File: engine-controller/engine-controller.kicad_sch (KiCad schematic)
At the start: 0 parts

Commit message: inital TCs
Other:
- added sheet TC0 (thermocouple.kicad_sch)
- added sheet TC1 (thermocouple.kicad_sch)
- added sheet TC2 (thermocouple.kicad_sch)
- added sheet TC3 (thermocouple.kicad_sch)
- sheet STM32 ports: added PA10, PA11, PA12, PA8, PA9, PB12, PB13, PB14, PB15, PB5, PB6, PB7, PB8, PB9, PC0, PC1, PC2, PC3, PC6, PC7, PC8, PC9, SPI1_MISO, SPI1_MOSI, SPI1_NSS, SPI1_SCK; removed none

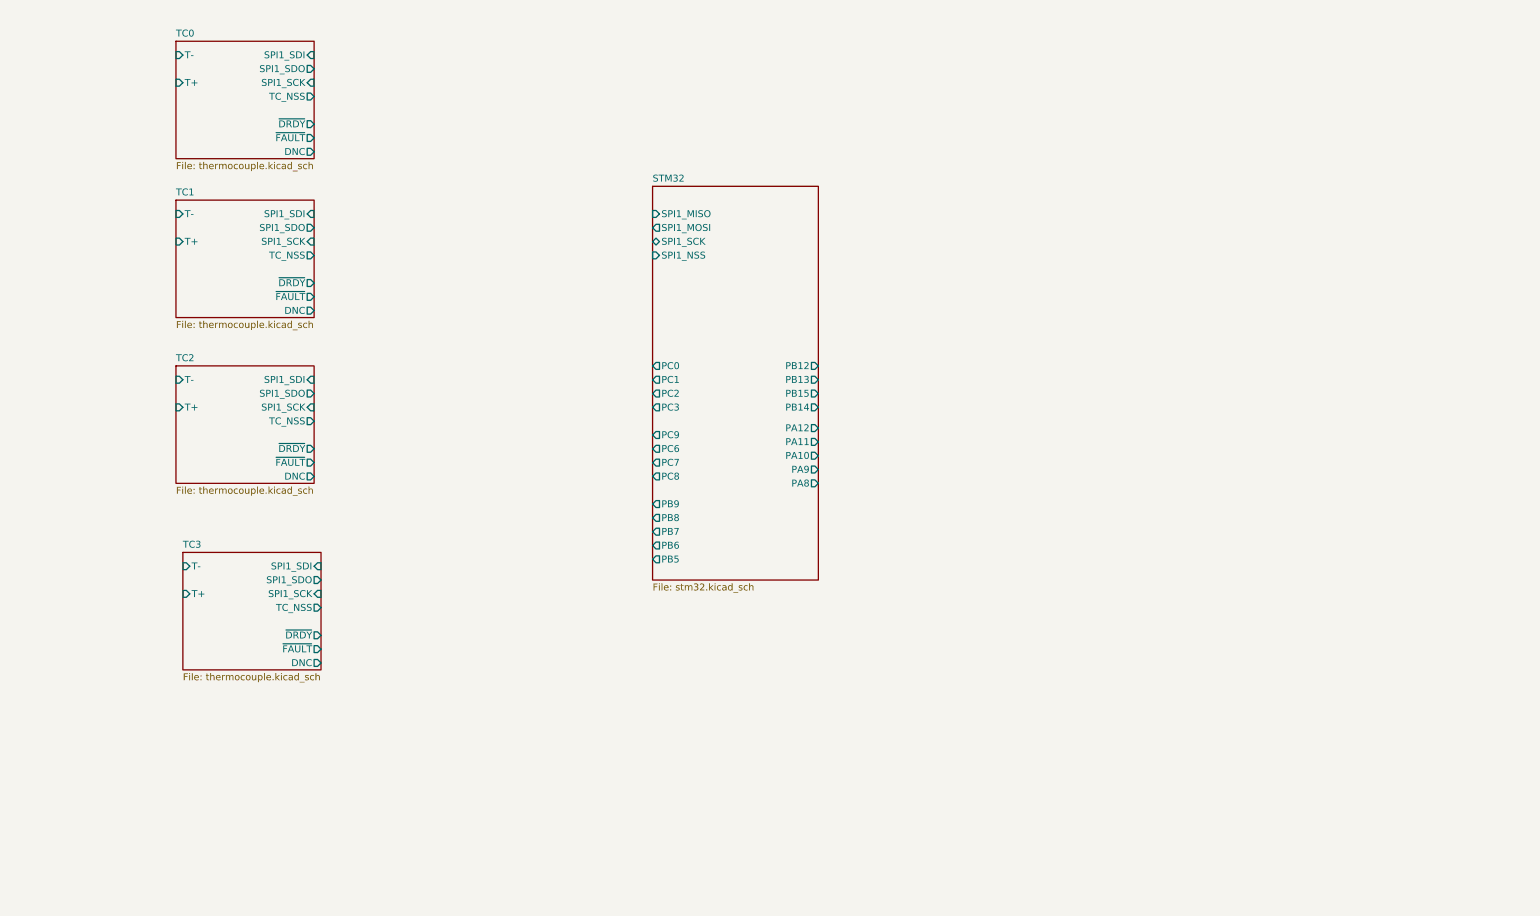
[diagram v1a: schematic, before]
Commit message: added 4-20mA sense circuit
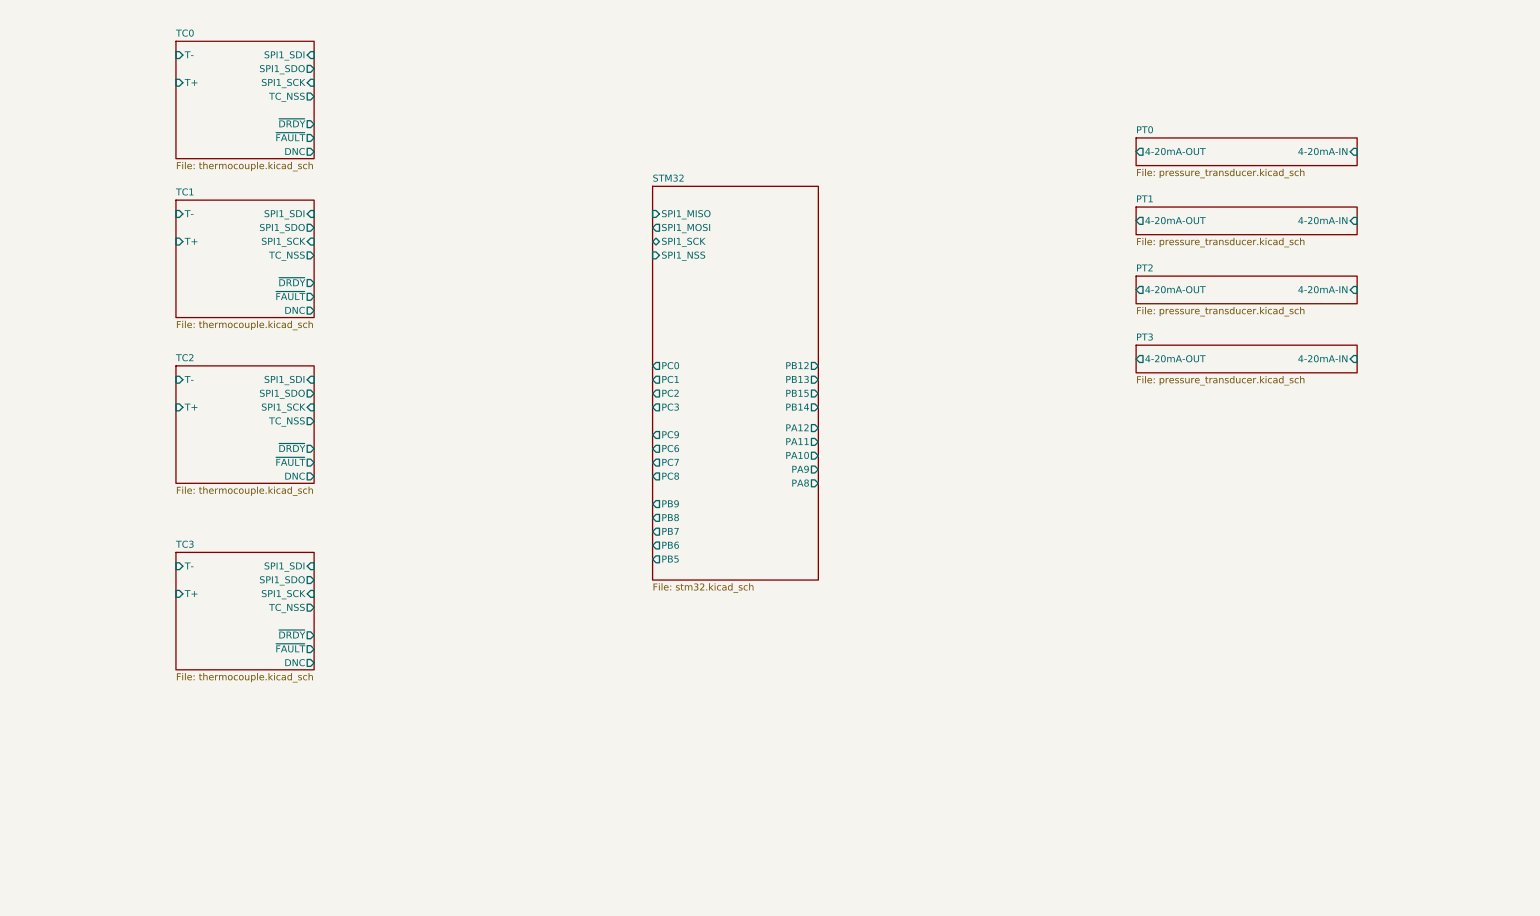
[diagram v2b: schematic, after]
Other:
- added sheet PT0 (pressure_transducer.kicad_sch)
- added sheet PT1 (pressure_transducer.kicad_sch)
- added sheet PT2 (pressure_transducer.kicad_sch)
- added sheet PT3 (pressure_transducer.kicad_sch)
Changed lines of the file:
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@@
 (kicad_sch (version 20230121) (generator eeschema)
   (paper "A4")
+  (sheet (at 215.9 64.77) (size 40.64 5.08) (fields_autoplaced)
+    (stroke (width 0.1524) (type solid))
+    (fill (color 252 255 135 1.0000))
+    (property "Sheetname" "PT2" (at 215.9 64.0584 0)
+      (effects (font (size 1.27 1.27)) (justify left bottom))
+    )
+    (property "Sheetfile" "pressure_transducer.kicad_sch" (at 215.9 70.4346 0)
+      (effects (font (size 1.27 1.27)) (justify left top))
+    )
+    (pin "4-20mA-OUT" output (at 215.9 67.31 180)
+      (effects (font (size 1.27 1.27)) (justify left))
+    )
+    (pin "4-20mA-IN" input (at 256.54 67.31 0)
+      (effects (font (size 1.27 1.27)) (justify right))
+    )
+    (instances
+      (project "engine-controller"
+        (path "/c646003c-e1a1-4f96-833a-f6a146234064" (page "9"))
+      )
+    )
+  )
   (sheet (at 39.37 21.59) (size 25.4 21.59) (fields_autoplaced)
     (stroke (width 0.1524) (type solid))
@@
     )
   )
+  (sheet (at 215.9 77.47) (size 40.64 5.08) (fields_autoplaced)
+    (stroke (width 0.1524) (type solid))
+    (fill (color 252 255 135 1.0000))
+    (property "Sheetname" "PT3" (at 215.9 76.7584 0)
+      (effects (font (size 1.27 1.27)) (justify left bottom))
+    )
+    (property "Sheetfile" "pressure_transducer.kicad_sch" (at 215.9 83.1346 0)
+      (effects (font (size 1.27 1.27)) (justify left top))
+    )
+    (pin "4-20mA-OUT" output (at 215.9 80.01 180)
+      (effects (font (size 1.27 1.27)) (justify left))
+    )
+    (pin "4-20mA-IN" input (at 256.54 80.01 0)
+      (effects (font (size 1.27 1.27)) (justify right))
+    )
+    (instances
+      (project "engine-controller"
+        (path "/c646003c-e1a1-4f96-833a-f6a146234064" (page "10"))
+      )
+    )
+  )
   (sheet (at 39.37 81.28) (size 25.4 21.59) (fields_autoplaced)
     (stroke (width 0.1524) (type solid))
@@
     )
   )
-  (sheet (at 40.64 115.57) (size 25.4 21.59) (fields_autoplaced)
+  (sheet (at 215.9 52.07) (size 40.64 5.08) (fields_autoplaced)
+    (stroke (width 0.1524) (type solid))
+    (fill (color 252 255 135 1.0000))
+    (property "Sheetname" "PT1" (at 215.9 51.3584 0)
+      (effects (font (size 1.27 1.27)) (justify left bottom))
+    )
+    (property "Sheetfile" "pressure_transducer.kicad_sch" (at 215.9 57.7346 0)
+      (effects (font (size 1.27 1.27)) (justify left top))
+    )
+    (pin "4-20mA-OUT" output (at 215.9 54.61 180)
+      (effects (font (size 1.27 1.27)) (justify left))
+    )
+    (pin "4-20mA-IN" input (at 256.54 54.61 0)
+      (effects (font (size 1.27 1.27)) (justify right))
+    )
+    (instances
+      (project "engine-controller"
+        (path "/c646003c-e1a1-4f96-833a-f6a146234064" (page "8"))
+      )
+    )
+  )
+  (sheet (at 39.37 115.57) (size 25.4 21.59) (fields_autoplaced)
     (stroke (width 0.1524) (type solid))
     (fill (color 208 255 173 1.0000))
-    (property "Sheetname" "TC3" (at 40.64 114.8584 0)
-      (effects (font (size 1.27 1.27)) (justify left bottom))
-    )
-    (property "Sheetfile" "thermocouple.kicad_sch" (at 40.64 137.7446 0)
-      (effects (font (size 1.27 1.27)) (justify left top))
-    )
-    (pin "T-" input (at 40.64 118.11 180)
-      (effects (font (size 1.27 1.27)) (justify left))
-    )
-    (pin "T+" input (at 40.64 123.19 180)
-      (effects (font (size 1.27 1.27)) (justify left))
-    )
-    (pin "SPI1_SCK" input (at 66.04 123.19 0)
-      (effects (font (size 1.27 1.27)) (justify right))
-    )
-    (pin "~{FAULT}" output (at 66.04 133.35 0)
-      (effects (font (size 1.27 1.27)) (justify right))
-    )
-    (pin "TC_NSS" output (at 66.04 125.73 0)
-      (effects (font (size 1.27 1.27)) (justify right))
-    )
-    (pin "~{DRDY}" output (at 66.04 130.81 0)
-      (effects (font (size 1.27 1.27)) (justify right))
-    )
-    (pin "DNC" output (at 66.04 135.89 0)
-      (effects (font (size 1.27 1.27)) (justify right))
-    )
-    (pin "SPI1_SDI" input (at 66.04 118.11 0)
-      (effects (font (size 1.27 1.27)) (justify right))
-    )
-    (pin "SPI1_SDO" output (at 66.04 120.65 0)
+    (property "Sheetname" "TC3" (at 39.37 114.8584 0)
+      (effects (font (size 1.27 1.27)) (justify left bottom))
+    )
+    (property "Sheetfile" "thermocouple.kicad_sch" (at 39.37 137.7446 0)
+      (effects (font (size 1.27 1.27)) (justify left top))
+    )
+    (pin "T-" input (at 39.37 118.11 180)
+      (effects (font (size 1.27 1.27)) (justify left))
+    )
+    (pin "T+" input (at 39.37 123.19 180)
+      (effects (font (size 1.27 1.27)) (justify left))
+    )
+    (pin "SPI1_SCK" input (at 64.77 123.19 0)
+      (effects (font (size 1.27 1.27)) (justify right))
+    )
+    (pin "~{FAULT}" output (at 64.77 133.35 0)
+      (effects (font (size 1.27 1.27)) (justify right))
+    )
+    (pin "TC_NSS" output (at 64.77 125.73 0)
+      (effects (font (size 1.27 1.27)) (justify right))
+    )
+    (pin "~{DRDY}" output (at 64.77 130.81 0)
+      (effects (font (size 1.27 1.27)) (justify right))
+    )
+    (pin "DNC" output (at 64.77 135.89 0)
+      (effects (font (size 1.27 1.27)) (justify right))
+    )
+    (pin "SPI1_SDI" input (at 64.77 118.11 0)
+      (effects (font (size 1.27 1.27)) (justify right))
+    )
+    (pin "SPI1_SDO" output (at 64.77 120.65 0)
       (effects (font (size 1.27 1.27)) (justify right))
     )
@@
       )
     )
+  )
+  (sheet (at 215.9 39.37) (size 40.64 5.08) (fields_autoplaced)
+    (stroke (width 0.1524) (type solid))
+    (fill (color 252 255 135 1.0000))
+    (property "Sheetname" "PT0" (at 215.9 38.6584 0)
+      (effects (font (size 1.27 1.27)) (justify left bottom))
+    )
+    (property "Sheetfile" "pressure_transducer.kicad_sch" (at 215.9 45.0346 0)
+      (effects (font (size 1.27 1.27)) (justify left top))
+    )
+    (pin "4-20mA-OUT" output (at 215.9 41.91 180)
+      (effects (font (size 1.27 1.27)) (justify left))
+    )
+    (pin "4-20mA-IN" input (at 256.54 41.91 0)
+      (effects (font (size 1.27 1.27)) (justify right))
+    )
+    (instances
+      (project "engine-controller"
+        (path "/c646003c-e1a1-4f96-833a-f6a146234064" (page "7"))
+      )
+    )

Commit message: added switches
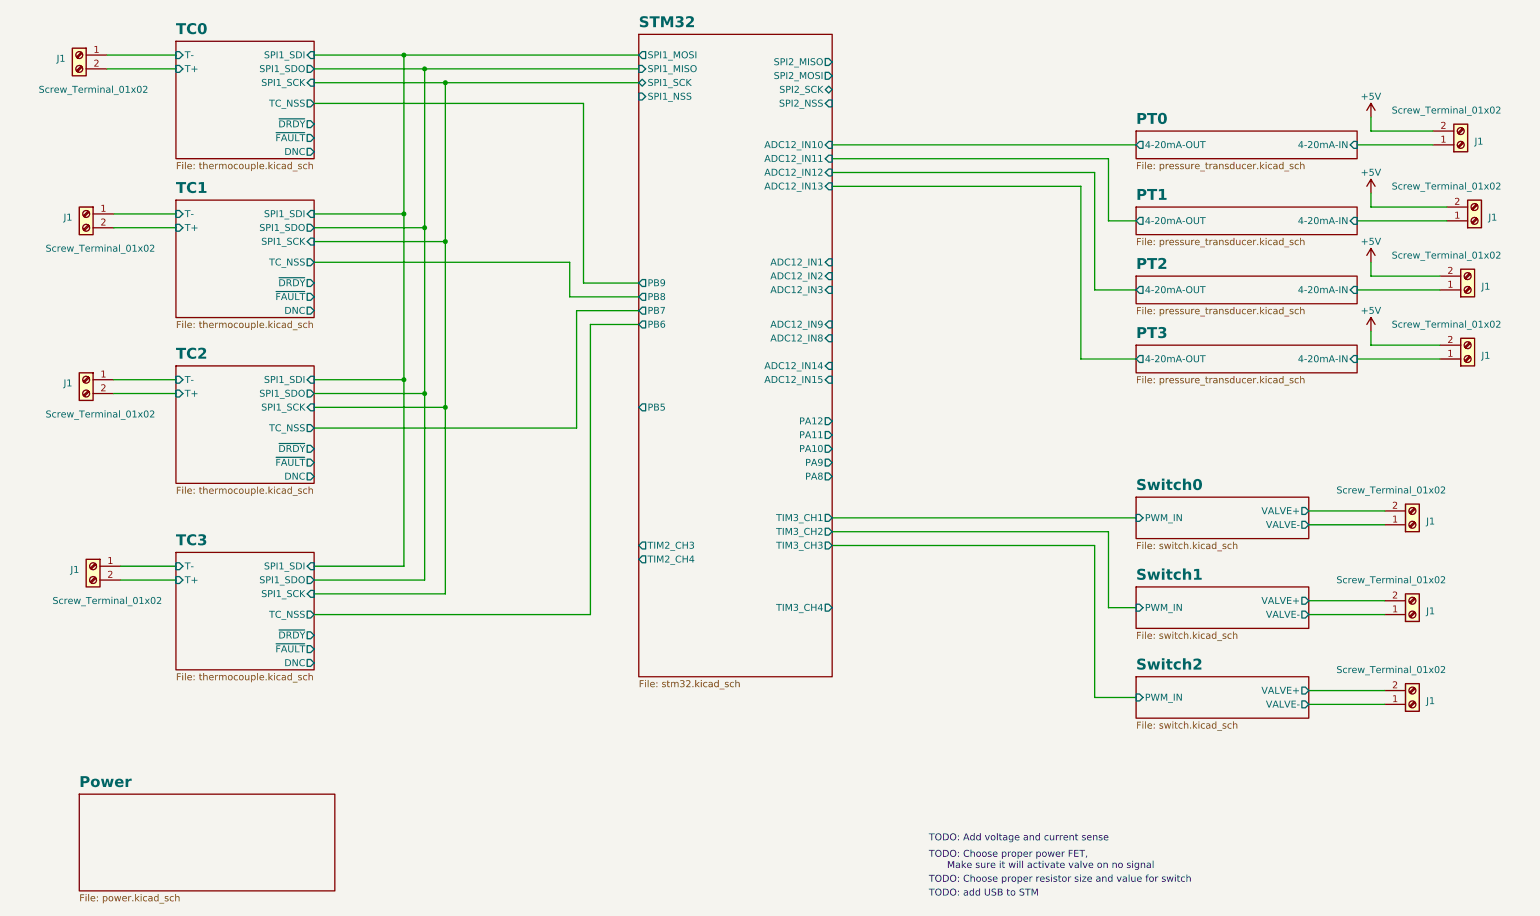
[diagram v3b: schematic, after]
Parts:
- added J1 (x11): Screw_Terminal_01x02, TerminalBlock_Phoenix:TerminalBlock_Phoenix_MKDS-1,5-2_1x02_P5.00mm_Horizontal, symbol Connector:Screw_Terminal_01x02
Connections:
- net PT0/4-20mA-IN: now also J1.1 (Pin_1)
- net PT1/4-20mA-IN: now also J1.1 (Pin_1)
- net PT2/4-20mA-IN: now also J1.1 (Pin_1)
- net PT3/4-20mA-IN: now also J1.1 (Pin_1)
- net TC0/T+: now also J1.2 (Pin_2)
- net TC0/T-: now also J1.1 (Pin_1)
- net TC1/T+: now also J1.2 (Pin_2)
- net TC1/T-: now also J1.1 (Pin_1)
- net TC2/T+: now also J1.2 (Pin_2)
- net TC2/T-: now also J1.1 (Pin_1)
- net TC3/T+: now also J1.2 (Pin_2)
- net TC3/T-: now also J1.1 (Pin_1)
- new net +5V: J1.2 (Pin_2), J1.2 (Pin_2), J1.2 (Pin_2), J1.2 (Pin_2)
- new net Switch0/VALVE+: J1.2 (Pin_2)
- new net Switch0/VALVE-: J1.1 (Pin_1)
- new net Switch1/VALVE+: J1.2 (Pin_2)
- new net Switch1/VALVE-: J1.1 (Pin_1)
- new net Switch2/VALVE+: J1.2 (Pin_2)
- new net Switch2/VALVE-: J1.1 (Pin_1)
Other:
- added sheet Power (power.kicad_sch)
- added sheet Switch0 (switch.kicad_sch)
- added sheet Switch1 (switch.kicad_sch)
- added sheet Switch2 (switch.kicad_sch)
- sheet STM32 ports: added ADC12_IN1, ADC12_IN10, ADC12_IN11, ADC12_IN12, ADC12_IN13, ADC12_IN14, ADC12_IN15, ADC12_IN2, ADC12_IN3, ADC12_IN8, ADC12_IN9, SPI2_MISO, SPI2_MOSI, SPI2_NSS, SPI2_SCK, TIM2_CH3, TIM2_CH4, TIM3_CH1, TIM3_CH2, TIM3_CH3, TIM3_CH4; removed PB12, PB13, PB14, PB15, PC0, PC1, PC2, PC3, PC6, PC7, PC8, PC9
- note added: "TODO: Add voltage and current sense"
- note added: "TODO: Choose proper power FET, Make sure it will activate valve on no signal"
- note added: "TODO: Choose proper resistor size and value for switch"
- note added: "TODO: add USB to STM"
